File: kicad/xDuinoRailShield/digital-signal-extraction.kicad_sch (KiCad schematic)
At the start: 11 parts, among them Q1 T2N7002BK, U301 6N137, U302 EL817

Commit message: xXiaoCentralMini
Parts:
- C8: renamed from C301; now not fitted
- D6: renamed from D301; now not fitted
- R1, R2: footprint Resistor_SMD:R_0805_2012Metric_Pad1.20x1.40mm_HandSolder -> Resistor_SMD:R_0603_1608Metric_Pad0.98x0.95mm_HandSolder
- R3: renamed from R301; footprint Resistor_SMD:R_0805_2012Metric_Pad1.20x1.40mm_HandSolder -> Resistor_SMD:R_0603_1608Metric_Pad0.98x0.95mm_HandSolder; now not fitted
- R4: renamed from R302; footprint Resistor_SMD:R_0805_2012Metric_Pad1.20x1.40mm_HandSolder -> Resistor_SMD:R_0603_1608Metric_Pad0.98x0.95mm_HandSolder; now not fitted
- R5: renamed from R303; footprint Resistor_SMD:R_0805_2012Metric_Pad1.20x1.40mm_HandSolder -> Resistor_SMD:R_0603_1608Metric_Pad0.98x0.95mm_HandSolder
- R5: footprint Resistor_SMD:R_0805_2012Metric_Pad1.20x1.40mm_HandSolder -> Resistor_SMD:R_0603_1608Metric_Pad0.98x0.95mm_HandSolder; now fitted
- U4: renamed from U302; now not fitted
- renumbered U301 to U3
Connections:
- net DCC_0_1K3: now also C8.1, D6.1 (K), R3.2
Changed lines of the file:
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@@
-	)
-	(junction
-		(at 82.55 71.12)
-		(diameter 0)
-		(color 0 0 0 0)
 	)
 	(junction
@@
 	(wire
 		(pts
-			(xy 82.55 71.12) (xy 88.9 71.12)
-		)
-		(stroke
-			(width 0)
-			(type default)
-		)
-	)
-	(wire
-		(pts
 			(xy 50.8 63.5) (xy 57.15 63.5)
 		)
@@
 				)
 				(justify right)
+				(hide yes)
+			)
+		)
+	)
+	(global_label "DCC_0_1K3"
+		(shape output)
+		(at 88.9 63.5 0)
+		(fields_autoplaced yes)
+		(effects
+			(font
+				(size 1.27 1.27)
+			)
+			(justify left)
+		)
+		(property "Intersheetrefs" "${INTERSHEET_REFS}"
+			(at 102.624 63.5 0)
+			(effects
+				(font
+					(size 1.27 1.27)
+				)
+				(justify left)
 				(hide yes)
 			)
@@
 		(exclude_from_sim no)
 		(in_bom no)
-		(on_board yes)
+		(on_board no)
 		(dnp yes)
 		(property "Reference" "R1"
@@
 			)
 		)
-		(property "Footprint" "Resistor_SMD:R_0805_2012Metric_Pad1.20x1.40mm_HandSolder"
+		(property "Footprint" "Resistor_SMD:R_0603_1608Metric_Pad0.98x0.95mm_HandSolder"
 			(at 168.148 66.04 90)
 			(effects
@@
 			(project "xDuinoRailShield"
 				(path "/e63e39d7-6ac0-4ffd-8aa3-1841a4541b55/b84a333b-f29e-43df-b84d-edef752a64aa"
-					(reference "R304")
+					(reference "R6")
 					(unit 1)
 				)
@@
 		(exclude_from_sim no)
 		(in_bom yes)
-		(on_board yes)
-		(dnp no)
-		(fields_autoplaced yes)
-		(property "Reference" "#PWR0303"
+		(on_board no)
+		(dnp yes)
+		(fields_autoplaced yes)
+		(property "Reference" "#PWR020"
 			(at 74.93 162.56 0)
 			(effects
@@
 			(project "xDuinoRailShield"
 				(path "/e63e39d7-6ac0-4ffd-8aa3-1841a4541b55/b84a333b-f29e-43df-b84d-edef752a64aa"
-					(reference "#PWR0303")
+					(reference "#PWR020")
 					(unit 1)
 				)
@@
 		(exclude_from_sim no)
 		(in_bom no)
-		(on_board yes)
+		(on_board no)
 		(dnp yes)
 		(property "Reference" "Q1"
@@
 			(project "xDuinoRailShield"
 				(path "/e63e39d7-6ac0-4ffd-8aa3-1841a4541b55/b84a333b-f29e-43df-b84d-edef752a64aa"
-					(reference "Q301")
+					(reference "Q1")
 					(unit 1)
 				)
@@
 		(exclude_from_sim no)
 		(in_bom yes)
-		(on_board yes)
-		(dnp no)
-		(property "Reference" "D301"
+		(on_board no)
+		(dnp yes)
+		(property "Reference" "D6"
 			(at 80.01 66.04 90)
 			(effects
@@
 			(project "xDuinoRailShield"
 				(path "/e63e39d7-6ac0-4ffd-8aa3-1841a4541b55/b84a333b-f29e-43df-b84d-edef752a64aa"
-					(reference "D301")
+					(reference "D6")
 					(unit 1)
 				)
@@
 		(exclude_from_sim no)
 		(in_bom yes)
-		(on_board yes)
-		(dnp no)
-		(fields_autoplaced yes)
-		(property "Reference" "#PWR0301"
+		(on_board no)
+		(dnp yes)
+		(fields_autoplaced yes)
+		(property "Reference" "#PWR018"
 			(at 74.93 97.79 0)
 			(effects
@@
 			(project "xDuinoRailShield"
 				(path "/e63e39d7-6ac0-4ffd-8aa3-1841a4541b55/b84a333b-f29e-43df-b84d-edef752a64aa"
-					(reference "#PWR0301")
+					(reference "#PWR018")
 					(unit 1)
 				)
@@
 		(exclude_from_sim no)
 		(in_bom yes)
-		(on_board yes)
+		(on_board no)
 		(dnp yes)
 		(fields_autoplaced yes)
-		(property "Reference" "R303"
+		(property "Reference" "R5"
 			(at 83.82 100.33 90)
 			(effects
@@
 			)
 		)
-		(property "Footprint" "Resistor_SMD:R_0805_2012Metric_Pad1.20x1.40mm_HandSolder"
+		(property "Footprint" "Resistor_SMD:R_0603_1608Metric_Pad0.98x0.95mm_HandSolder"
 			(at 83.82 104.902 90)
 			(effects
@@
 			(project "xDuinoRailShield"
 				(path "/e63e39d7-6ac0-4ffd-8aa3-1841a4541b55/b84a333b-f29e-43df-b84d-edef752a64aa"
-					(reference "R303")
+					(reference "R5")
 					(unit 1)
 				)
@@
 		(exclude_from_sim no)
 		(in_bom yes)
-		(on_board yes)
-		(dnp no)
-		(fields_autoplaced yes)
-		(property "Reference" "#PWR0304"
+		(on_board no)
+		(dnp yes)
+		(fields_autoplaced yes)
+		(property "Reference" "#PWR021"
 			(at 76.2 123.19 0)
 			(effects
@@
 			(project "xDuinoRailShield"
 				(path "/e63e39d7-6ac0-4ffd-8aa3-1841a4541b55/b84a333b-f29e-43df-b84d-edef752a64aa"
-					(reference "#PWR0304")
+					(reference "#PWR021")
 					(unit 1)
 				)
@@
 		(exclude_from_sim no)
 		(in_bom yes)
-		(on_board yes)
-		(dnp no)
-		(fields_autoplaced yes)
-		(property "Reference" "#PWR0302"
+		(on_board no)
+		(dnp yes)
+		(fields_autoplaced yes)
+		(property "Reference" "#PWR019"
 			(at 74.93 149.86 0)
 			(effects
@@
 			(project "xDuinoRailShield"
 				(path "/e63e39d7-6ac0-4ffd-8aa3-1841a4541b55/b84a333b-f29e-43df-b84d-edef752a64aa"
-					(reference "#PWR0302")
+					(reference "#PWR019")
 					(unit 1)
 				)
@@
 		(exclude_from_sim no)
 		(in_bom yes)
-		(on_board yes)
+		(on_board no)
 		(dnp no)
 		(property "Reference" "#PWR08"
@@
 			(project "xDuinoRailShield"
 				(path "/e63e39d7-6ac0-4ffd-8aa3-1841a4541b55/b84a333b-f29e-43df-b84d-edef752a64aa"
-					(reference "#PWR0305")
+					(reference "#PWR022")
 					(unit 1)
 				)
@@
 		(exclude_from_sim no)
 		(in_bom yes)
-		(on_board yes)
-		(dnp no)
-		(fields_autoplaced yes)
-		(property "Reference" "U302"
+		(on_board no)
+		(dnp yes)
+		(fields_autoplaced yes)
+		(property "Reference" "U4"
 			(at 66.04 142.24 0)
 			(effects
@@
 			(project "xDuinoRailShield"
 				(path "/e63e39d7-6ac0-4ffd-8aa3-1841a4541b55/b84a333b-f29e-43df-b84d-edef752a64aa"
-					(reference "U302")
+					(reference "U4")
 					(unit 1)
 				)
@@
 		(exclude_from_sim no)
 		(in_bom yes)
-		(on_board yes)
-		(dnp no)
-		(fields_autoplaced yes)
-		(property "Reference" "R302"
+		(on_board no)
+		(dnp yes)
+		(fields_autoplaced yes)
+		(property "Reference" "R4"
 			(at 78.74 142.24 90)
 			(effects
@@
 			)
 		)
-		(property "Footprint" "Resistor_SMD:R_0805_2012Metric_Pad1.20x1.40mm_HandSolder"
+		(property "Footprint" "Resistor_SMD:R_0603_1608Metric_Pad0.98x0.95mm_HandSolder"
 			(at 78.74 146.812 90)
 			(effects
@@
 			(project "xDuinoRailShield"
 				(path "/e63e39d7-6ac0-4ffd-8aa3-1841a4541b55/b84a333b-f29e-43df-b84d-edef752a64aa"
-					(reference "R302")
+					(reference "R4")
 					(unit 1)
 				)
@@
 		(exclude_from_sim no)
 		(in_bom yes)
-		(on_board yes)
-		(dnp no)
-		(property "Reference" "C301"
+		(on_board no)
+		(dnp yes)
+		(property "Reference" "C8"
 			(at 64.77 66.04 0)
 			(effects
@@
 			(project "xDuinoRailShield"
 				(path "/e63e39d7-6ac0-4ffd-8aa3-1841a4541b55/b84a333b-f29e-43df-b84d-edef752a64aa"
-					(reference "C301")
+					(reference "C8")
 					(unit 1)
 				)
@@
 		(exclude_from_sim no)
 		(in_bom no)
-		(on_board yes)
+		(on_board no)
 		(dnp yes)
 		(property "Reference" "R2"
@@
 			)
 		)
-		(property "Footprint" "Resistor_SMD:R_0805_2012Metric_Pad1.20x1.40mm_HandSolder"
+		(property "Footprint" "Resistor_SMD:R_0603_1608Metric_Pad0.98x0.95mm_HandSolder"
 			(at 168.148 78.74 90)
 			(effects
@@
 			(project "xDuinoRailShield"
 				(path "/e63e39d7-6ac0-4ffd-8aa3-1841a4541b55/b84a333b-f29e-43df-b84d-edef752a64aa"
-					(reference "R305")
+					(reference "R7")
 					(unit 1)
 				)
@@
 		(in_bom no)
 		(on_board yes)
-		(dnp yes)
+		(dnp no)
 		(fields_autoplaced yes)
 		(property "Reference" "R5"
@@
 			)
 		)
-		(property "Footprint" "Resistor_SMD:R_0805_2012Metric_Pad1.20x1.40mm_HandSolder"
+		(property "Footprint" "Resistor_SMD:R_0603_1608Metric_Pad0.98x0.95mm_HandSolder"
 			(at 176.53 118.618 90)
 			(effects
@@
 			(project "xDuinoRailShield"
 				(path "/e63e39d7-6ac0-4ffd-8aa3-1841a4541b55/b84a333b-f29e-43df-b84d-edef752a64aa"
-					(reference "R306")
+					(reference "R8")
 					(unit 1)
 				)
@@
 		(exclude_from_sim no)
 		(in_bom yes)
-		(on_board yes)
-		(dnp no)
-		(fields_autoplaced yes)
-		(property "Reference" "R301"
+		(on_board no)
+		(dnp yes)
+		(fields_autoplaced yes)
+		(property "Reference" "R3"
 			(at 60.96 57.15 90)
 			(effects
@@
 			)
 		)
-		(property "Footprint" "Resistor_SMD:R_0805_2012Metric_Pad1.20x1.40mm_HandSolder"
+		(property "Footprint" "Resistor_SMD:R_0603_1608Metric_Pad0.98x0.95mm_HandSolder"
 			(at 60.96 65.278 90)
 			(effects
@@
 			(project "xDuinoRailShield"
 				(path "/e63e39d7-6ac0-4ffd-8aa3-1841a4541b55/b84a333b-f29e-43df-b84d-edef752a64aa"
-					(reference "R301")
+					(reference "R3")
 					(unit 1)
 				)
@@
 		(exclude_from_sim no)
 		(in_bom no)
-		(on_board yes)
+		(on_board no)
 		(dnp yes)
 		(fields_autoplaced yes)
-		(property "Reference" "U301"
+		(property "Reference" "U3"
 			(at 66.04 99.06 0)
 			(effects
@@
 			(project "xDuinoRailShield"
 				(path "/e63e39d7-6ac0-4ffd-8aa3-1841a4541b55/b84a333b-f29e-43df-b84d-edef752a64aa"
-					(reference "U301")
-					(unit 1)
-				)
+					(reference "U3")
+					(unit 1)
+				)

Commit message: More nice changes
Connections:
- net DCC_MM_SIGNAL is gone; now on net +5V: Q1.3 (D), R4.1, R5.1, R5.2, U3.6 (VO)
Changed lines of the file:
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@@
 	(paper "A4")
+	(junction
+		(at 74.93 140.97)
+		(diameter 0)
+		(color 0 0 0 0)
+	)
 	(junction
 		(at 68.58 71.12)
@@
 	)
 	(junction
+		(at 74.93 148.59)
+		(diameter 0)
+		(color 0 0 0 0)
+	)
+	(junction
 		(at 166.37 87.63)
 		(diameter 0)
@@
 	)
 	(junction
-		(at 74.93 148.59)
-		(diameter 0)
-		(color 0 0 0 0)
-	)
-	(junction
 		(at 166.37 90.17)
 		(diameter 0)
@@
 	(wire
 		(pts
-			(xy 74.93 146.05) (xy 74.93 148.59)
+			(xy 74.93 140.97) (xy 74.93 148.59)
 		)
 		(stroke
@@
 	(wire
 		(pts
+			(xy 74.93 139.7) (xy 74.93 140.97)
+		)
+		(stroke
+			(width 0)
+			(type default)
+		)
+	)
+	(wire
+		(pts
 			(xy 74.93 156.21) (xy 74.93 153.67)
 		)
@@
 	(wire
 		(pts
-			(xy 82.55 148.59) (xy 85.09 148.59)
+			(xy 74.93 148.59) (xy 85.09 148.59)
 		)
 		(stroke
@@
 	)
 	(label "Optocopler Low-Speed (PC817)"
-		(at 43.18 137.16 0)
+		(at 39.37 133.35 0)
 		(fields_autoplaced yes)
 		(effects
@@
 		(lib_name "+5V_1")
 		(lib_id "power:+5V")
-		(at 74.93 146.05 0)
+		(at 74.93 139.7 0)
 		(unit 1)
 		(exclude_from_sim no)
@@
 		(fields_autoplaced yes)
 		(property "Reference" "#PWR019"
-			(at 74.93 149.86 0)
+			(at 74.93 143.51 0)
 			(effects
 				(font
@@
 		)
 		(property "Value" "+5V"
-			(at 74.93 140.97 0)
+			(at 74.93 134.62 0)
 			(effects
 				(font
@@
 		)
 		(property "Footprint" ""
-			(at 74.93 146.05 0)
+			(at 74.93 139.7 0)
 			(effects
 				(font
@@
 		)
 		(property "Datasheet" ""
-			(at 74.93 146.05 0)
+			(at 74.93 139.7 0)
 			(effects
 				(font
@@
 		)
 		(property "Description" ""
-			(at 74.93 146.05 0)
+			(at 74.93 139.7 0)
 			(effects
 				(font
@@
 	)
 	(symbol
-		(lib_id "Device:R")
-		(at 78.74 148.59 270)
-		(unit 1)
-		(exclude_from_sim no)
-		(in_bom yes)
-		(on_board no)
-		(dnp yes)
-		(fields_autoplaced yes)
-		(property "Reference" "R4"
-			(at 78.74 142.24 90)
-			(effects
-				(font
-					(size 1.27 1.27)
-				)
-			)
-		)
-		(property "Value" "220R"
-			(at 78.74 144.78 90)
-			(effects
-				(font
-					(size 1.27 1.27)
-				)
-			)
-		)
-		(property "Footprint" "Resistor_SMD:R_0603_1608Metric_Pad0.98x0.95mm_HandSolder"
-			(at 78.74 146.812 90)
-			(effects
-				(font
-					(size 1.27 1.27)
-				)
-				(hide yes)
-			)
-		)
-		(property "Datasheet" "~"
-			(at 78.74 148.59 0)
-			(effects
-				(font
-					(size 1.27 1.27)
-				)
-				(hide yes)
-			)
-		)
-		(property "Description" ""
-			(at 78.74 148.59 0)
-			(effects
-				(font
-					(size 1.27 1.27)
-				)
-				(hide yes)
-			)
-		)
-		(property "LCSC" "C17557"
-			(at 78.74 148.59 0)
-			(effects
-				(font
-					(size 1.27 1.27)
-				)
-				(hide yes)
-			)
-		)
-		(pin "2"
-		)
-		(pin "1"
-		)
-		(instances
-			(project "xDuinoRailShield"
-				(path "/e63e39d7-6ac0-4ffd-8aa3-1841a4541b55/b84a333b-f29e-43df-b84d-edef752a64aa"
-					(reference "R4")
-					(unit 1)
-				)
-			)
-		)
-	)
-	(symbol
 		(lib_id "Device:C")
 		(at 68.58 67.31 0)
@@
 					(unit 1)
 				)
+			)
+		)
+	)
+	(symbol
+		(lib_id "Device:R")
+		(at 74.93 144.78 0)
+		(unit 1)
+		(exclude_from_sim no)
+		(in_bom yes)
+		(on_board no)
+		(dnp yes)
+		(fields_autoplaced yes)
+		(property "Reference" "R4"
+			(at 77.47 143.5099 0)
+			(effects
+				(font
+					(size 1.27 1.27)
+				)
+				(justify left)
+			)
+		)
+		(property "Value" "220R"
+			(at 77.47 146.0499 0)
+			(effects
+				(font
+					(size 1.27 1.27)
+				)
+				(justify left)
+			)
+		)
+		(property "Footprint" "Resistor_SMD:R_0603_1608Metric_Pad0.98x0.95mm_HandSolder"
+			(at 73.152 144.78 90)
+			(effects
+				(font
+					(size 1.27 1.27)
+				)
+				(hide yes)
+			)
+		)
+		(property "Datasheet" "~"
+			(at 74.93 144.78 0)
+			(effects
+				(font
+					(size 1.27 1.27)
+				)
+				(hide yes)
+			)
+		)
+		(property "Description" ""
+			(at 74.93 144.78 0)
+			(effects
+				(font
+					(size 1.27 1.27)
+				)
+				(hide yes)
+			)
+		)
+		(property "LCSC" "C17557"
+			(at 74.93 144.78 0)
+			(effects
+				(font
+					(size 1.27 1.27)
+				)
+				(hide yes)
+			)
+		)
+		(pin "2"
+		)
+		(pin "1"
+		)
+		(instances
+			(project "xDuinoRailShield"
+				(path "/e63e39d7-6ac0-4ffd-8aa3-1841a4541b55/b84a333b-f29e-43df-b84d-edef752a64aa"
+					(reference "R4")
+					(unit 1)
+				)

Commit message: More busses added
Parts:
- renumbered C8 to C401, D6 to D401, R3 to R401, R4 to R402, R5 to R403, U3 to U401, U4 to U402
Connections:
- net +5V: no longer Q1.3 (D), R402.2, R403.1, R5.2, U401.6 (VO), U402.4
- net DCC_1 renamed DCC1
- net DCC­_0 renamed DCC0
- new net DCC_MM_SIGNAL: Q1.3 (D), R402.2, R403.1, R5.2, U401.6 (VO), U402.4
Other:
- moved on the sheet: R402

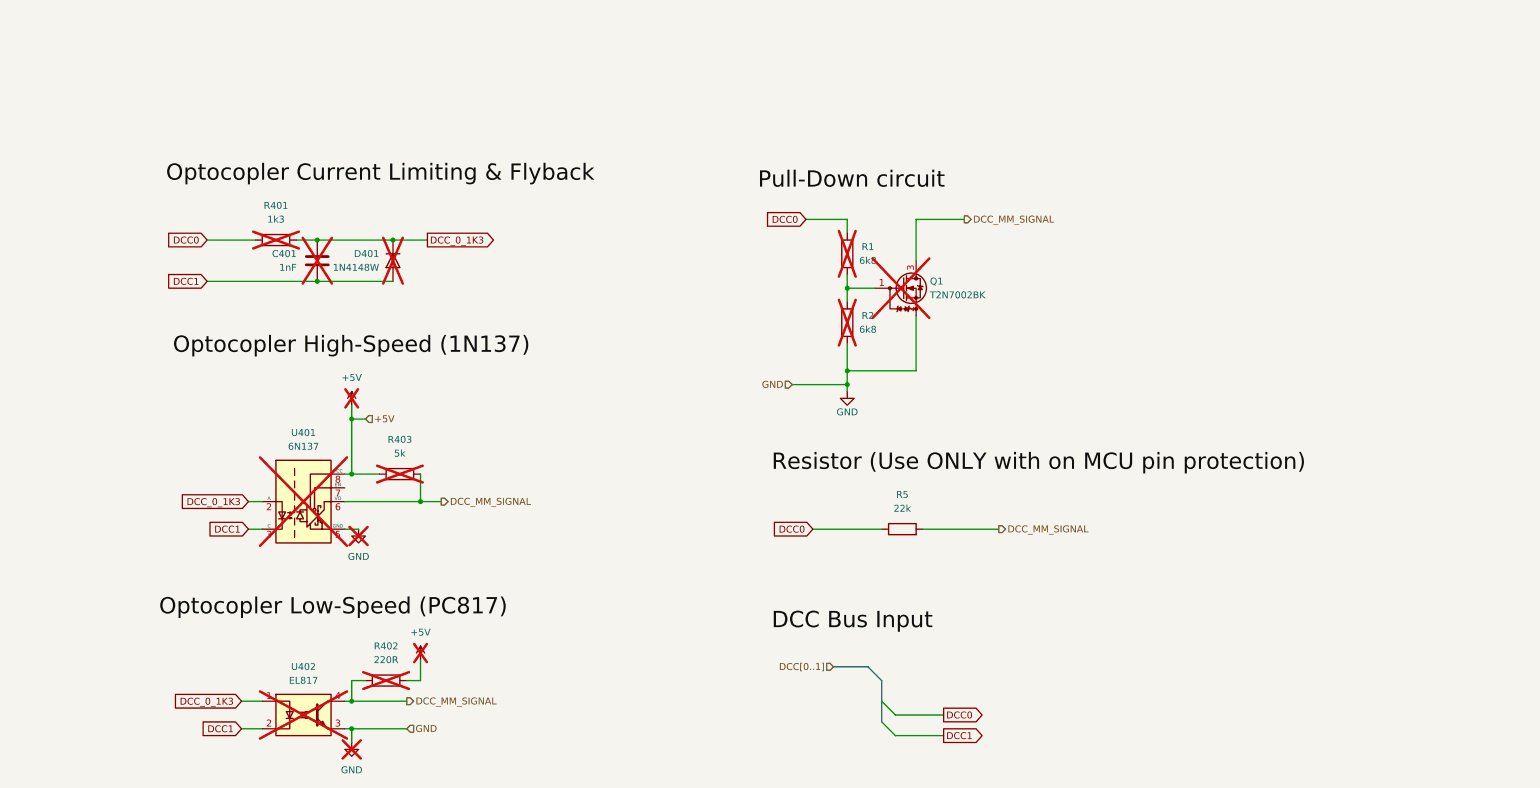
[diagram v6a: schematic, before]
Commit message: Draft of loco decoder
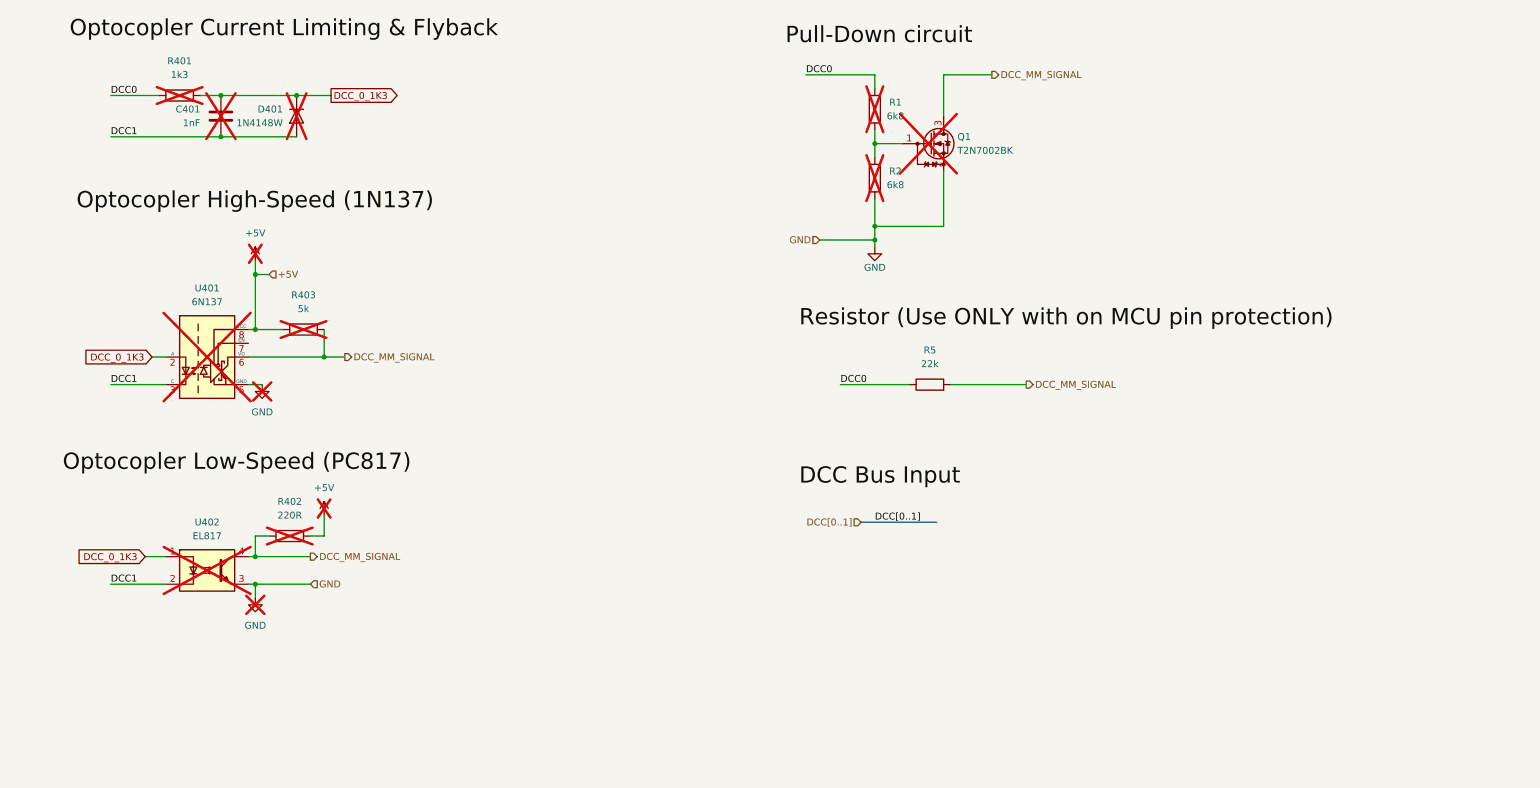
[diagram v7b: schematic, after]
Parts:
- C401, D401, R401, R402, R403, U402: now left out of the parts list
- R5: footprint Resistor_SMD:R_0603_1608Metric_Pad0.98x0.95mm_HandSolder -> Resistor_SMD:R_0805_2012Metric_Pad1.20x1.40mm_HandSolder
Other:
- moved on the sheet: C401, D401, Q1, R1, R2, R401, R402, R403, R5, U401, U402

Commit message: A lot of fixes
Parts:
- R1, R2: footprint Resistor_SMD:R_0603_1608Metric_Pad0.98x0.95mm_HandSolder -> Resistor_SMD:R_0805_2012Metric_Pad1.20x1.40mm_HandSolder
- R301: renamed from R401; footprint Resistor_SMD:R_0603_1608Metric_Pad0.98x0.95mm_HandSolder -> Resistor_SMD:R_0805_2012Metric_Pad1.20x1.40mm_HandSolder
- R302: renamed from R402; footprint Resistor_SMD:R_0603_1608Metric_Pad0.98x0.95mm_HandSolder -> Resistor_SMD:R_0805_2012Metric_Pad1.20x1.40mm_HandSolder
- R303: renamed from R403; footprint Resistor_SMD:R_0603_1608Metric_Pad0.98x0.95mm_HandSolder -> Resistor_SMD:R_0805_2012Metric_Pad1.20x1.40mm_HandSolder
- U302: renamed from U402; footprint Package_DIP:DIP-4_W8.89mm_SMDSocket_LongPads -> Package_DIP:DIP-4_W7.62mm
- renumbered C401 to C301, D401 to D301, U401 to U301
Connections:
- net +5V: now also U301.7 (EN)
- no-connect marks 0 -> 2
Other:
- note added: "DCC Bus Input"
- note added: "Optocopler Current Limiting & Flyback"
- note added: "Optocopler High-Speed (1N137)"
- note added: "Optocopler Low-Speed (PC817)"
- note added: "Pull-Down circuit"
- note added: "Resistor (Use ONLY with on MCU pin protection)"
- company: (none) -> Chatelain Engineering
- title: (none) -> Digital Signal Extraction
- moved on the sheet: Q1, R1, R2, R303, R5
